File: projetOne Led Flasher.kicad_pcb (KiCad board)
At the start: 2 copper layers, 41.9 x 25.4 mm, 14 parts, among them J1 jack, U1 NE555D

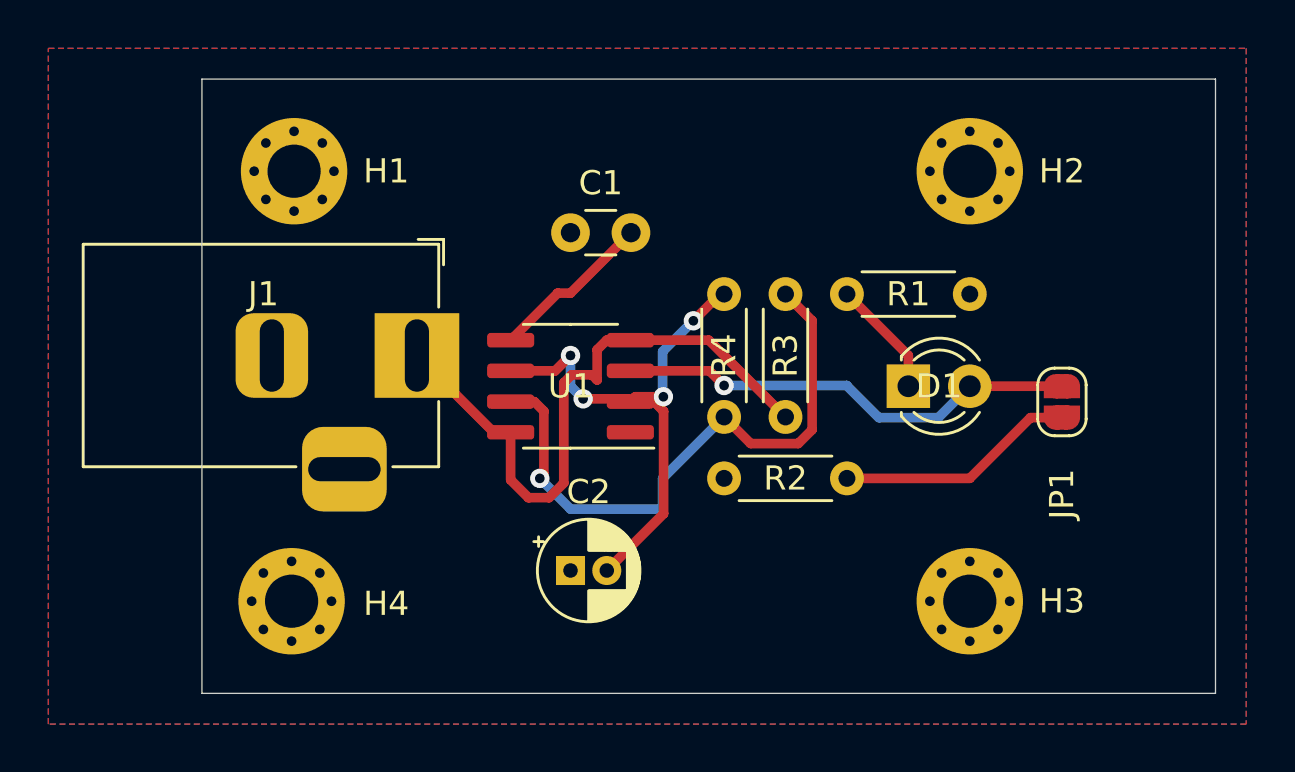
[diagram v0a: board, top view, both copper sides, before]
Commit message: Added Externelal libraries
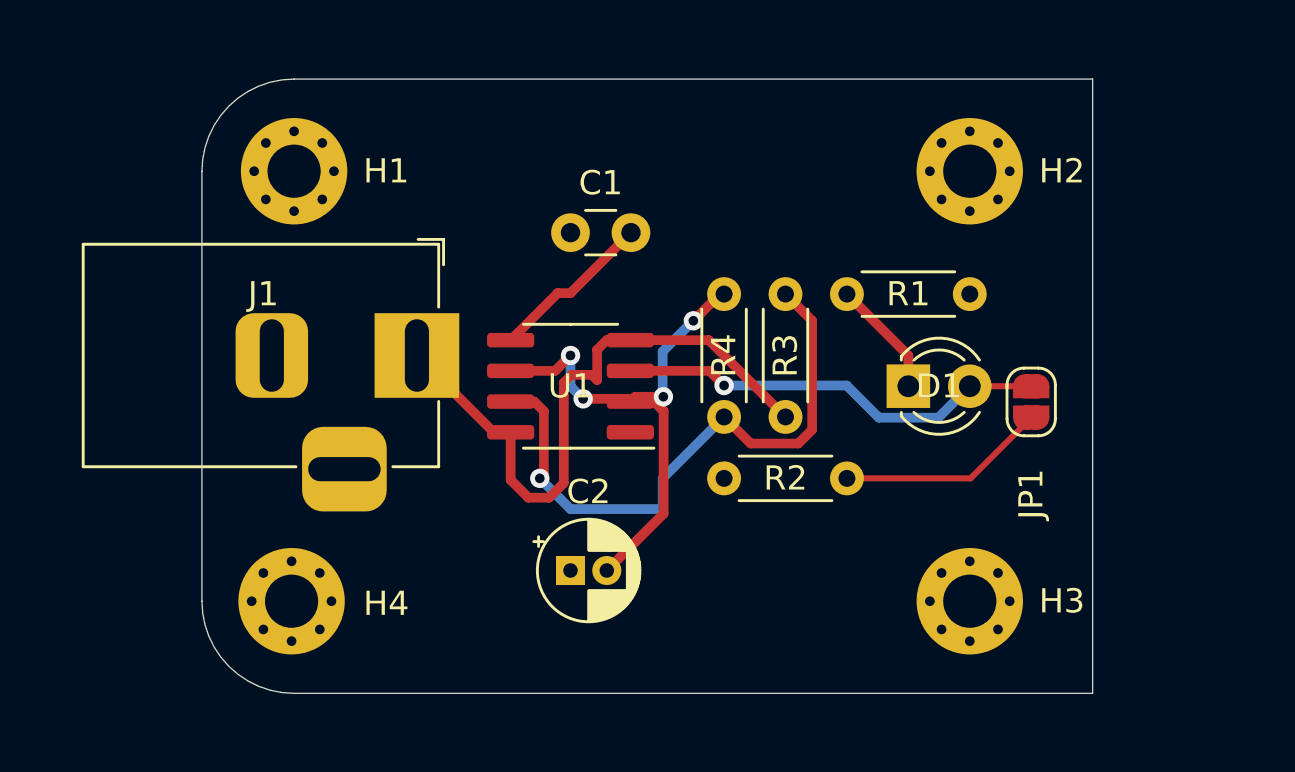
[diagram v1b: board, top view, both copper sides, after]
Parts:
- moved JP1 1.27 mm to (95.2, 57.8)
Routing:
- net OUT: track 19.2 -> 17.9 mm
- net Net-(JP1-Pad2): track 9.93 -> 8.66 mm
- removed copper zone on B.Cu, net GND
- removed copper zone on F.Cu, net GND
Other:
- board size 41.9 x 25.4 mm -> 36.8 x 25.4 mm
